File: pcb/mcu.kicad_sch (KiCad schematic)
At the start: 38 parts, among them J2 Connector, USB-TYPE-C-16P, J3 ESPPROG, SW1 RST_SW, SW2 BOOT_SW, SW3 CFG_SW, U6 AHT20_C2757850, U7 TLV803SDBZR, U8 ESP32-C6-MINI-1

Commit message: feat: create pcb production files and swap some parts for basic
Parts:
- removed U6: AHT20_C2757850, EasyEDA:SENSOR-SMD_L3.0-W3.0-P1.00-BR, symbol EasyEDA:AHT20_C2757850
- added U6: AHT20-F, EasyEDA:SENSOR-SMD-6_AHT20, symbol EasyEDA:AHT20-F
- SW1: value RST_SW -> TS-1095PS-A1B2-C3D2
- SW2: value BOOT_SW -> TS-1095PS-A1B2-C3D2
- SW3: value CFG_SW -> TS-1095PS-A1B2-C3D2
- TP11: value MCU_RST -> RH-5001
- TP18: value MOSI -> TestPad; footprint TestPoint:TestPoint_Pad_1.0x1.0mm -> EasyEDA:TestPoint_Pad_1.0x1.0mm; now not fitted; now left out of the parts list
- TP19: value SCK -> TestPad; footprint TestPoint:TestPoint_Pad_1.0x1.0mm -> EasyEDA:TestPoint_Pad_1.0x1.0mm; now not fitted; now left out of the parts list
- TP20: value MISO -> TestPad; footprint TestPoint:TestPoint_Pad_1.0x1.0mm -> EasyEDA:TestPoint_Pad_1.0x1.0mm; now not fitted; now left out of the parts list
- TP21: value ETH_CS -> TestPad; footprint TestPoint:TestPoint_Pad_1.0x1.0mm -> EasyEDA:TestPoint_Pad_1.0x1.0mm; now not fitted; now left out of the parts list
- TP22: value ETH_INT -> TestPad; footprint TestPoint:TestPoint_Pad_1.0x1.0mm -> EasyEDA:TestPoint_Pad_1.0x1.0mm; now not fitted; now left out of the parts list
- TP23: value ETH_RST -> TestPad; footprint TestPoint:TestPoint_Pad_1.0x1.0mm -> EasyEDA:TestPoint_Pad_1.0x1.0mm; now not fitted; now left out of the parts list
- U8: value ESP32-C6-MINI-1 -> ESP32-C6-MINI-1U-H4; footprint EasyEDA:WIFIM-SMD_61P-L16.6-W13.2-P0.80-ESP32-C6-MINI-1-N4 -> EasyEDA:WIFIM-SMD_61P-L13.2-W12.5-P0.80; LCSC Part C5736265 -> C20627095; MPN ESP32-C6-MINI-1-N4 -> ESP32-C6-MINI-1U-H4
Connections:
- net +3V3: now also U6.2 (VDD)
- net GND: now also U6.5 (GND)
- net SCL: now also U6.3 (SCL)
- net SDA: now also U6.4 (SDA)

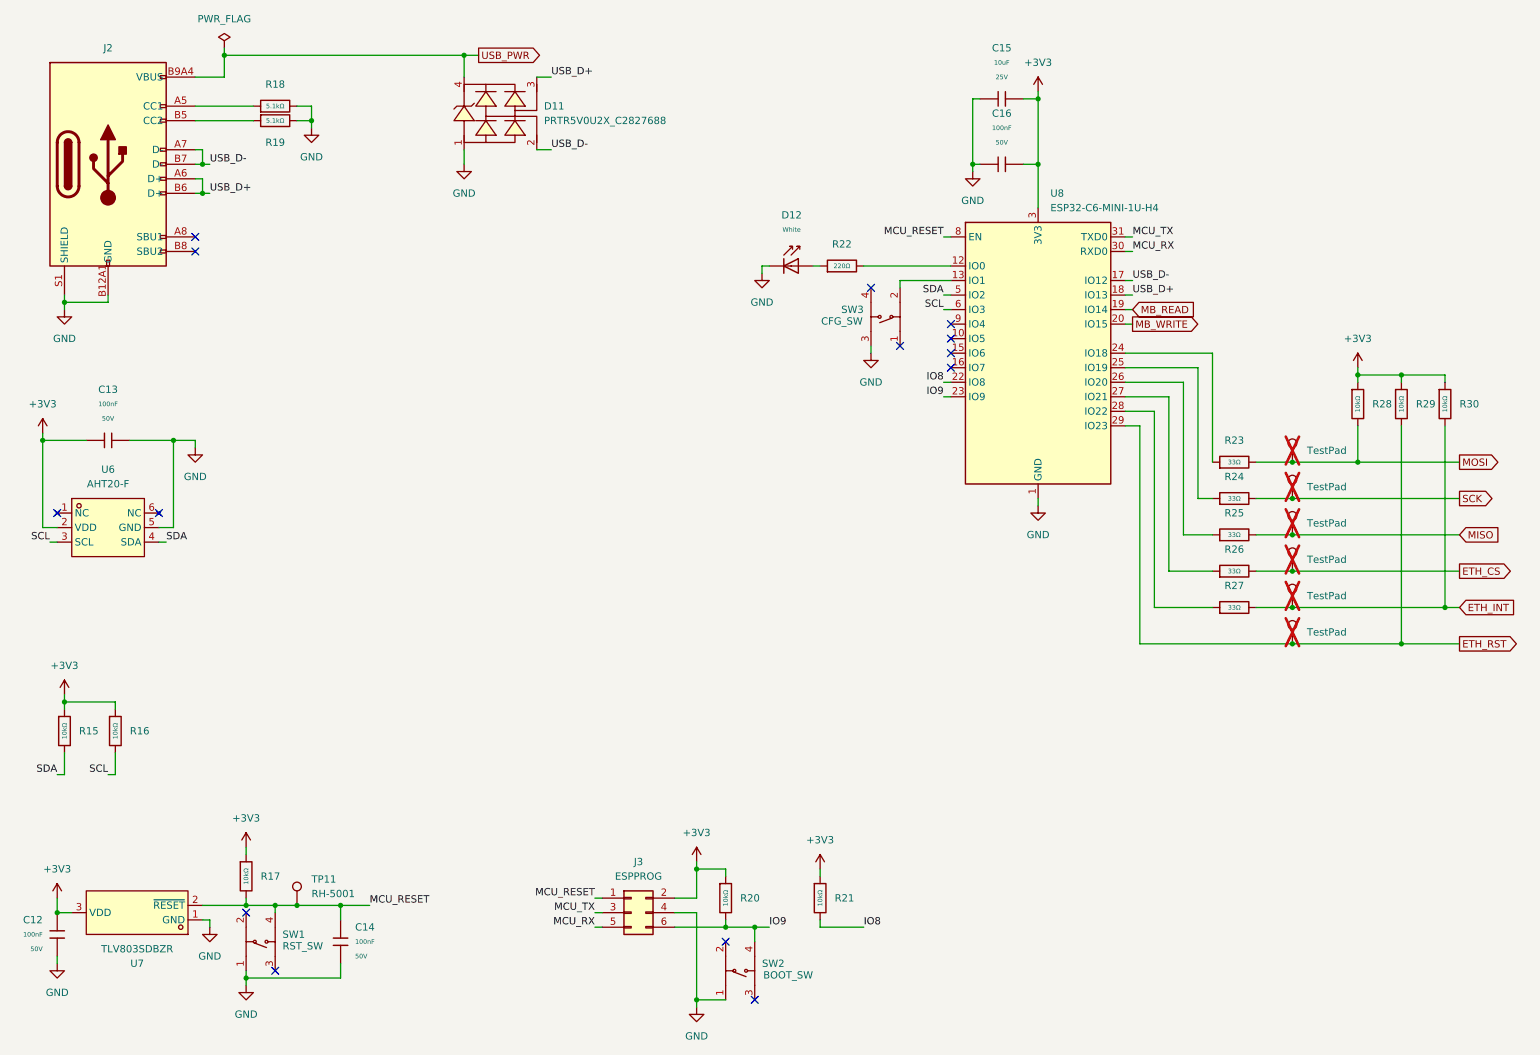
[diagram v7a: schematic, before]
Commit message: feat: replace many parts for basic parts
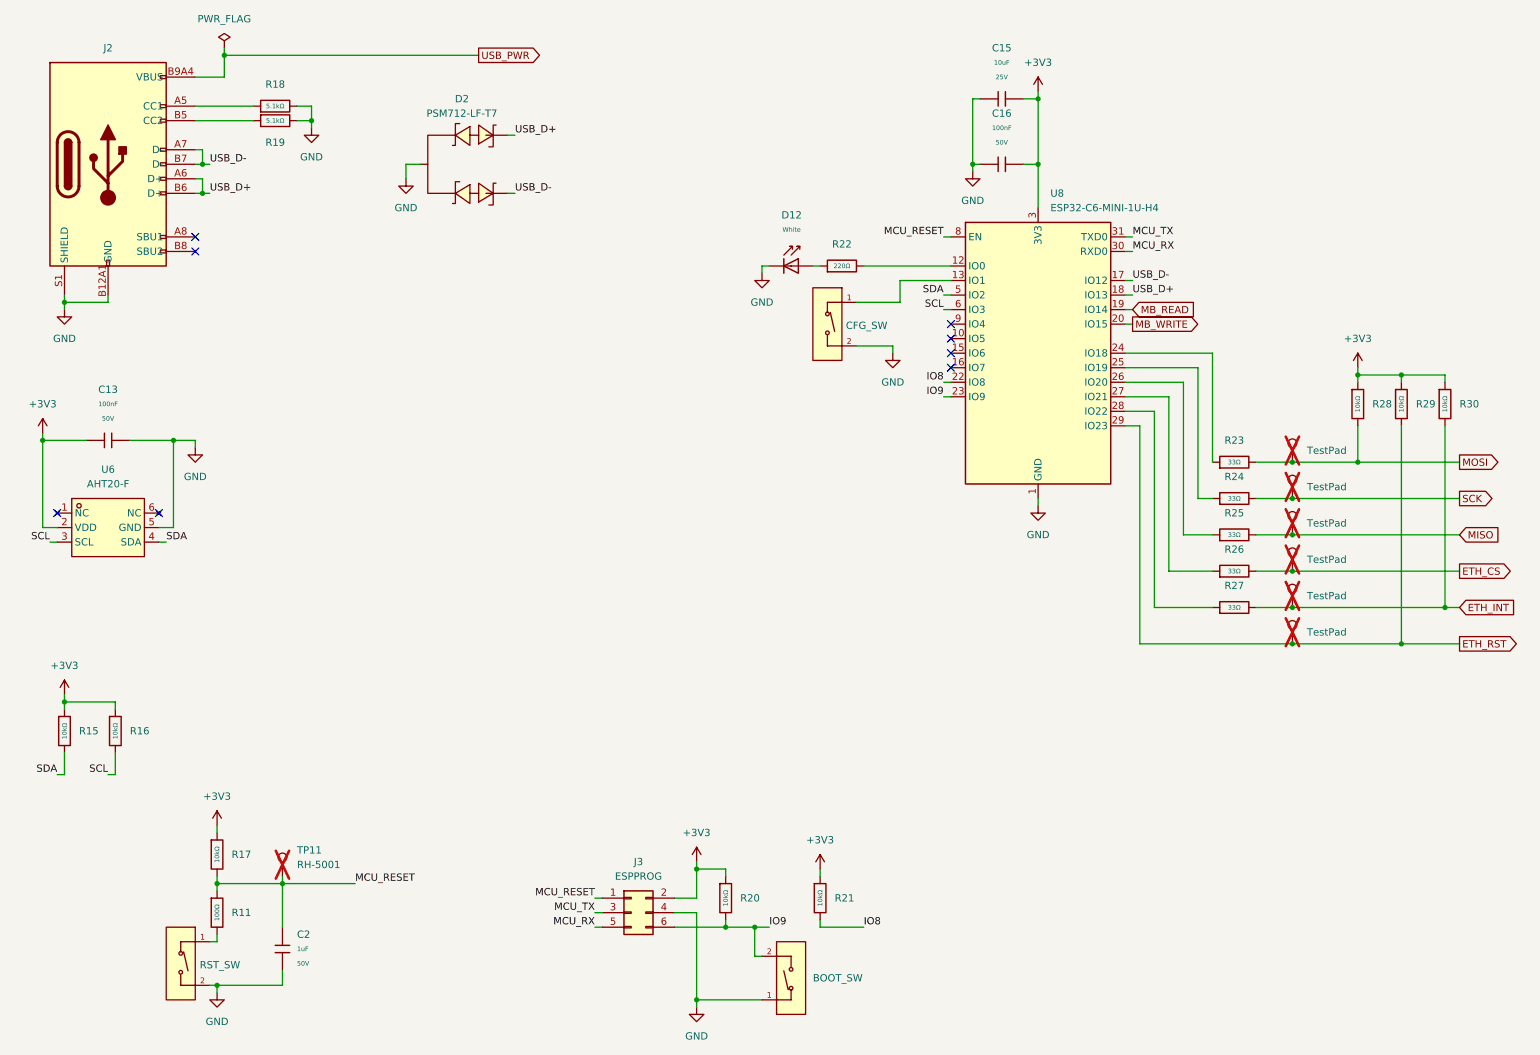
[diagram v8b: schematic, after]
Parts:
- removed C12, C14: 100nF, PCM_JLCPCB:C_0603, symbol PCM_JLCPCB-Capacitors:0603,100nF
- removed D11: PRTR5V0U2X_C2827688, EasyEDA:SOT-143-4_L2.9-W1.3-P1.92-LS2.4-BL, symbol EasyEDA:PRTR5V0U2X_C2827688
- removed SW1, SW2, SW3: TS-1095PS-A1B2-C3D2, EasyEDA:KEY-SMD_4P-L6.0-W6.0-P3.90-LS9.0, symbol EasyEDA:TS-1095PS-A1B2-C3D2
- removed U7: TLV803SDBZR, EasyEDA:SOT-23-3_L2.9-W1.3-P1.90-LS2.4-BR, symbol EasyEDA:TLV803SDBZR
- added C2: 1uF, PCM_JLCPCB:C_0603, symbol PCM_JLCPCB-Capacitors:0603,1uF
- added D2: PSM712-LF-T7, PCM_JLCPCB:SOT-23-3_L3.0-W1.7-P0.95-LS2.9-BR, symbol PCM_JLCPCB-Diode-Packages:TVS-Bi, PSM712-LF-T7
- added R11: 100Ω, PCM_JLCPCB:R_0603, symbol PCM_JLCPCB-Resistors:0603,100Ω
- added S1, S2, S3: Tactile Button, 160gf, PCM_JLCPCB:SW_TS-1088-AR02016, symbol PCM_JLCPCB-Connectors_Buttons:Tactile Button, 160gf, 12V, 50mA, 4.0mm
- TP11: now not fitted; now left out of the parts list
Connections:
- net GND: now also C2.2, D2.3 (K), S1.2 (B), S2.2 (B), S3.1 (A)
- net IO9: now also S3.2 (B)
- net MCU_RESET: now also C2.1, R11.1
- net USB_D+: now also D2.2 (A1)
- net USB_D-: now also D2.1 (A1)
- net at U8.13 (IO1): now also S1.1 (A)
- new net: R11.2, S2.1 (A)
- no-connect marks 14 -> 8
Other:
- moved on the sheet: R17
